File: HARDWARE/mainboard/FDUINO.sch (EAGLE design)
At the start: 68 parts, among them IC1 ATMEGA328PMA, IC2 LF50, IC3 L6205, Q1 CSM-7X-DU, SW1 SWITCHTHT, SW2 SWITCHTHT, SW3 SWITCHTHT, SW4 SWITCHTHT, T1 BPX81, T2 BPX81, T3 BPX81, T4 BPX81, T5 BPX81, T6 BPX81, T7 BPX81, T8 BPX81

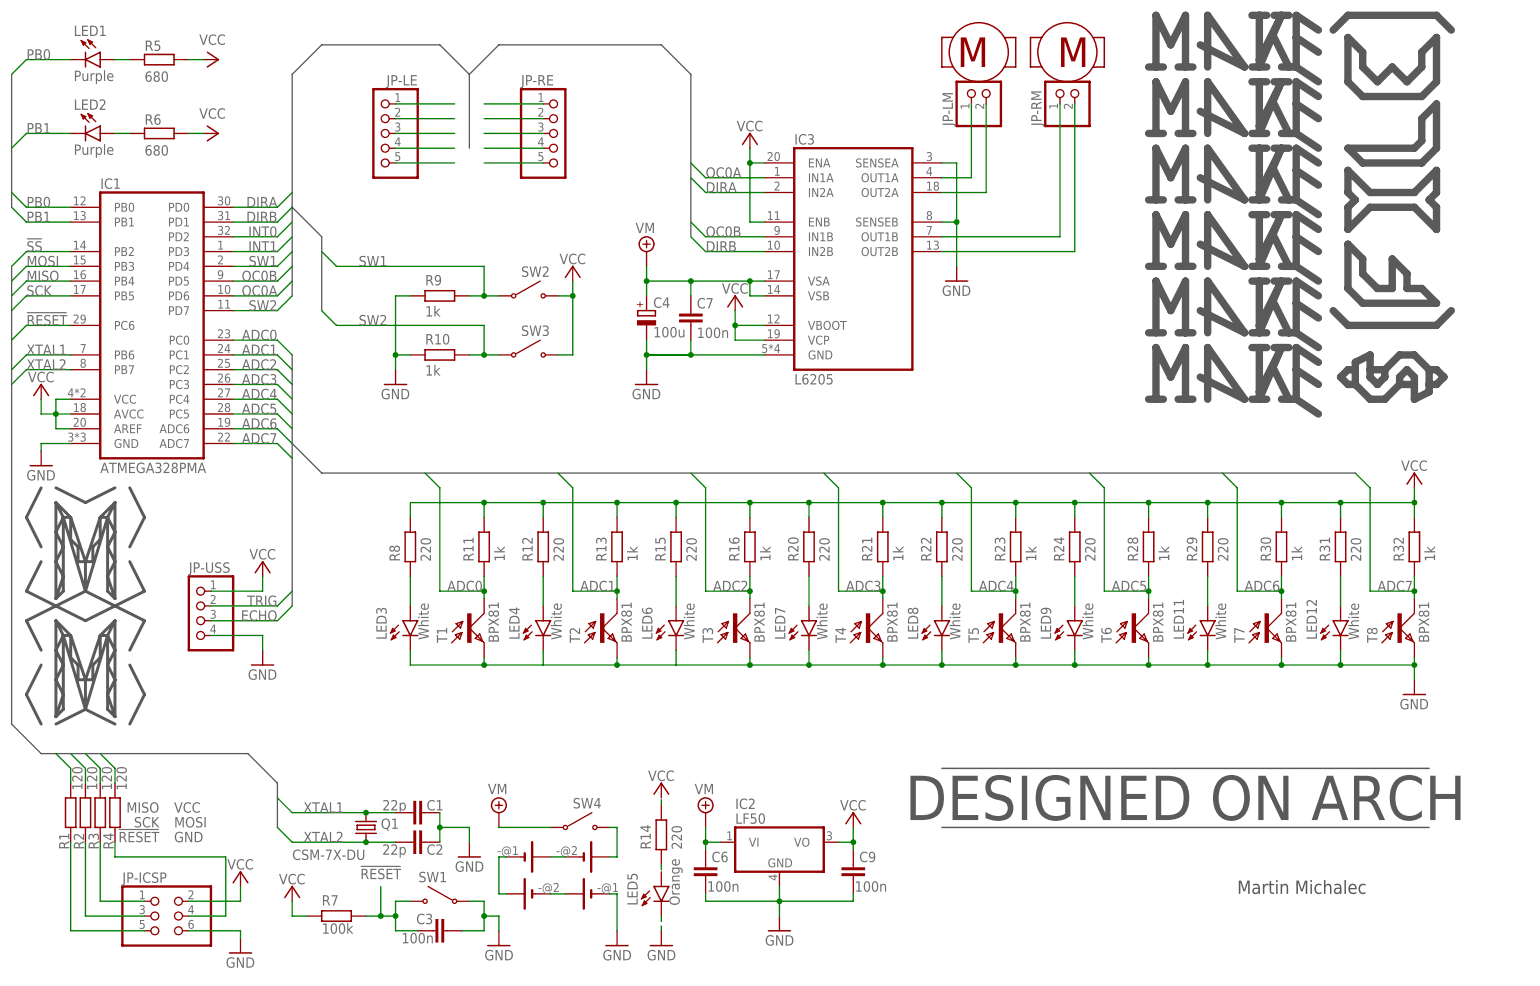
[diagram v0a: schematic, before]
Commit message: added UART connector, USR button, motor connectors, charge pump for motor driver
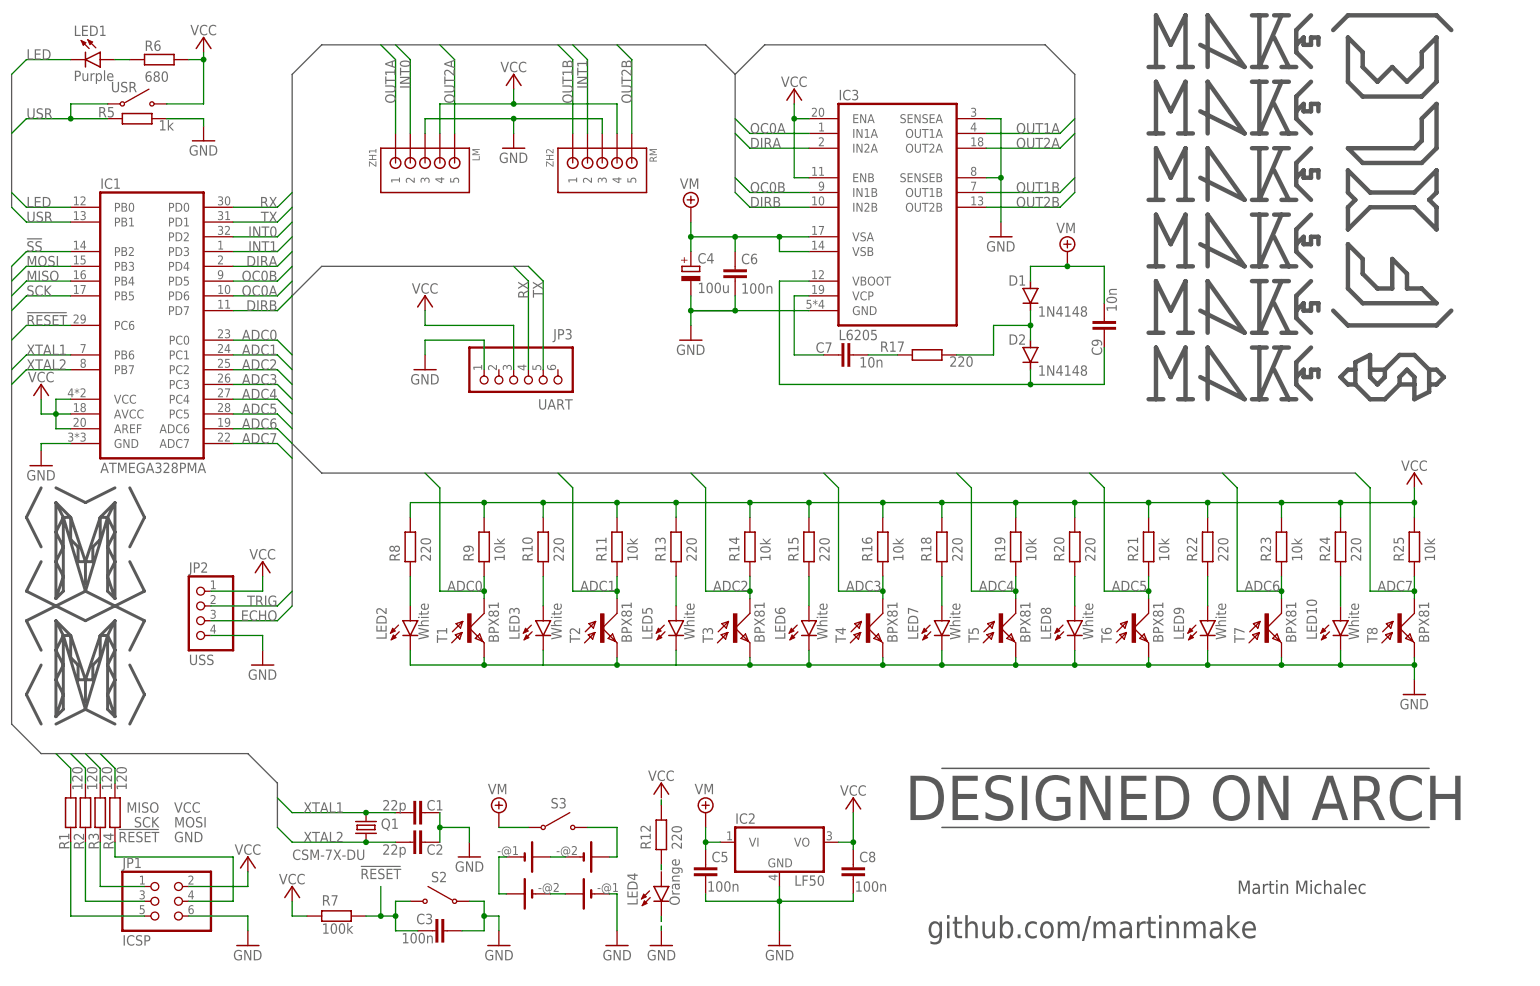
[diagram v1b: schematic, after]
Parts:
- removed JP-ICSP: (no value), pinhead:PINHD-2X3
- removed JP-LE, JP-RE: (no value), pinhead:PINHD-1X5
- removed JP-LM, JP-RM: (no value), pinhead:PINHD-1X2
- removed LED11: White, led:LEDSML1206
- removed R28, R30: 1k, rcl:R-EU_R1206
- removed R29, R31: 220, rcl:R-EU_R1206
- removed SW2, SW3, SW4: SWITCHTHT, martinmake:SWITCHTHT
- removed U$2, U$3: BAT, martinmake:BAT
- added BAT1, BAT2: BATSERIES, martinmake:BATSERIES
- added C5, C8: 100n, rcl:C-EUC1206
- added D1, D2: 1N4148, diode:1N4148DO35-7
- added JP1: ICSP, pinhead:PINHD-2X3
- added JP3: UART, pinhead:PINHD-1X6/90
- added R17, R18: 220, rcl:R-EU_R1206
- added R19: 10k, rcl:R-EU_R1206
- added S3, USR: SWITCHTHT, martinmake:SWITCHTHT
- added ZH1: LM, jst:B5B-ZR
- added ZH2: RM, jst:B5B-ZR
- C7, C9: value 100n -> 10n
- JP2: value (none) -> USS
- LED2: value Purple -> White
- LED4: value White -> Orange
- LED5: value Orange -> White
- R10, R13: value 1k -> 220
- R11, R16, R21, R23, R25, R9: value 1k -> 10k
- R14: value 220 -> 10k
- R5: value 680 -> 1k
- renumbered JP-USS to JP2, LED12 to LED10, R32 to R25, SW1 to S2
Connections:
- net PB0 renamed LED
- removed net N$12 (its old number): LED7.A, R20.2
- removed net N$13: JP-LE.5
- removed net N$26: JP-LE.4
- removed net N$29: JP-LE.3
- removed net N$31: JP-LE.2
- removed net N$34: JP-LE.1
- removed net N$36 (its old number): LED5.A, R14.2
- removed net N$37: JP-RE.1
- removed net N$38 (its old number): R29.1
- removed net N$39: JP-RE.3
- removed net N$41 (its old number): R31.1
- removed net N$42: R11.1, R13.1, R16.1, R21.1, R23.1, R25.1, R28.1, R30.1
- removed net N$44: JP-RE.2
- removed net N$46: JP-RE.5
- removed net N$48: JP-RE.4
- removed net N$6: IC3.OUT1B, JP-RM.1
- removed net N$8: IC3.OUT2A, JP-LM.2
- removed net PB1: IC1.PB1, LED2.C
- removed net SW1: IC1.PD4, R9.1, SW2.1
- removed net SW2: IC1.PD7, R10.1, SW3.1
- new net N$1: LED5.A, R13.2
- new net N$2: C9.1, D2.C, IC3.VBOOT
- new net N$28: R18.1
- new net N$32: R13.1
- new net N$43: LED3.A, R10.2
- new net OUT1A: IC3.OUT1A, ZH1.1
- new net OUT1B: IC3.OUT1B, ZH2.1
- new net OUT2A: IC3.OUT2A, ZH1.5
- new net OUT2B: IC3.OUT2B, ZH2.5
- new net RX: IC1.PD0, JP3.4
- new net TX: IC1.PD1, JP3.5
- new net USR: IC1.PB1, R5.1, USR.1
- net ADC0: now also R9.2; no longer R11.2
- net ADC1: now also R11.2; no longer R13.2
- net ADC2: now also R14.2; no longer R16.2
- net ADC3: now also R16.2; no longer R21.2
- net ADC4: now also R19.2; no longer R23.2
- net ADC5: now also R21.2; no longer R28.2
- net ADC6: now also R23.2; no longer R30.2
- net DIRA: now also IC1.PD4; no longer IC1.PD0
- net DIRB: now also IC1.PD7; no longer IC1.PD1
- net GND: now also BAT2A.-, C5.2, C8.2, JP1.6, JP3.1, LED4.C, R5.2, ZH1.3, ZH2.3; no longer C7.2, C9.2, JP-ICSP.6, LED5.C, R10.2, R9.2, U$3A.-
- net GND2: now also LED2.C, LED5.C; no longer LED11.C, LED4.C
- net INT0: now also ZH1.2
- net INT1: now also ZH2.2
- net N$10: now also BAT1A.+, BAT1B.-; no longer U$2A.+, U$2B.-
- net N$14: now also BAT1B.+, S3.2; no longer SW4.2, U$2B.+
- net N$15: now also BAT1A.-, BAT2B.+; no longer U$2A.-, U$3B.+
- net N$22: now also R24.2; no longer R31.2
- net N$23: now also LED7.A, R18.2; no longer LED8.A, R22.2
- net N$27: now also LED8.A, R20.2; no longer LED9.A, R24.2
- net N$3: now also D1.C, D2.A, R17.2; no longer IC3.OUT2B, JP-RM.2
- net N$30: now also LED9.A, R22.2; no longer LED11.A, R29.2
- net N$33: now also JP1.1; no longer JP-ICSP.1
- net N$4: now also C7.2, R17.1; no longer LED2.A, R6.1
- net N$40: now also R10.1; no longer R12.1
- net N$47: now also LED2.A; no longer LED3.A
- net N$49: now also JP1.3; no longer JP-ICSP.3
- net N$5: now also R6.1; no longer R5.1
- net N$50: now also JP1.5; no longer JP-ICSP.5
- net N$51: now also JP1.4; no longer JP-ICSP.4
- net N$7: now also C7.1, IC3.VCP; no longer IC3.OUT1A, JP-LM.1
- net N$9: now also BAT2A.+, BAT2B.-; no longer U$3A.+, U$3B.-
- net VCC: now also C8.1, JP1.2, JP3.3, R11.1, R12.1, R16.1, R19.1, R21.1, R23.1, R25.1, R9.1, USR.2, ZH1.4, ZH2.4; no longer C9.1, IC3.VBOOT, IC3.VCP, JP-ICSP.2, R5.2, SW2.2, SW3.2
- net VM: now also C5.1, C9.2, D1.A, S3.1; no longer C7.1, SW4.1
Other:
- note added: "LED and Button"
- note added: "Line Sensors"
- note added: "Motors with Encoders"
- note added: "Uart"
- note added: "github.com/martinmake"
- note removed: "Buttons"
- note removed: "Encoders"
- note removed: "LEDs"
- note removed: "Line sensors"
- note removed: "Motors"
- moved on the sheet: C4, C6, C7, C9, IC3, LED2, LED3, LED4, LED5, LED6, LED7, LED8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
